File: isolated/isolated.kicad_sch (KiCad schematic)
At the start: 59 parts, among them J1 Screw_Terminal_01x02, J2 Screw_Terminal_01x02, Q1 IRLIZ 34N, Q2 IRLIZ 34N, U1 LTC3723, U2 TCMT1103, U3 TL431DBZ

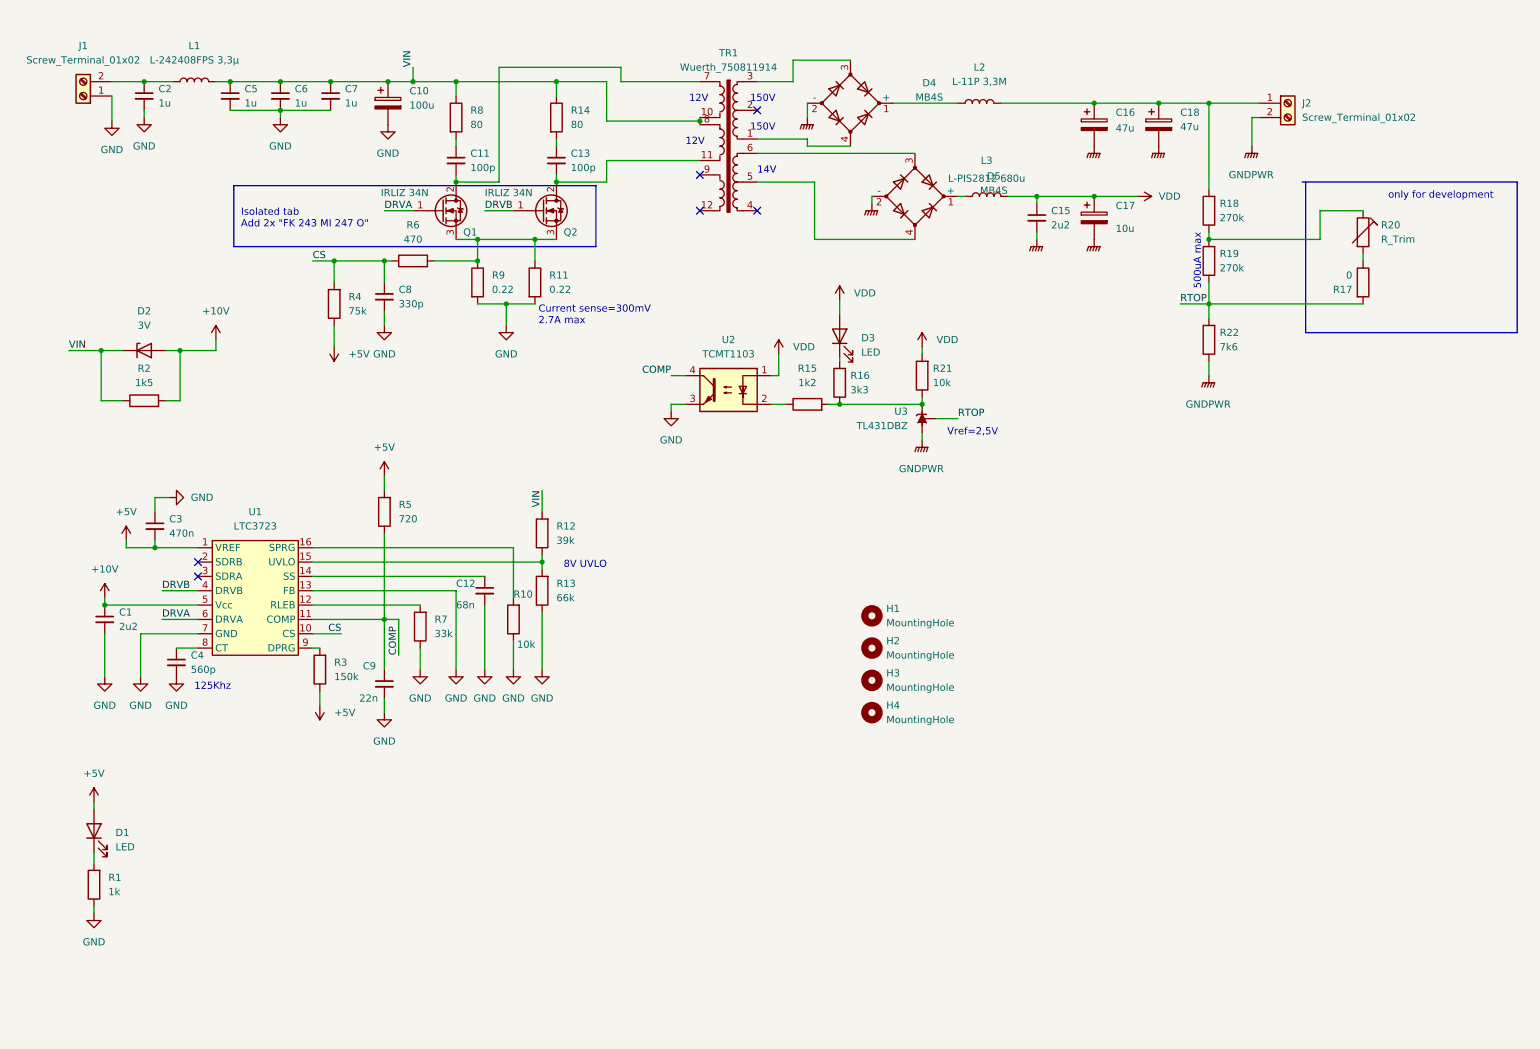
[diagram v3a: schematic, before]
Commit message: doc/kicad: Update to revision v0.2
Fix the problems found in revision v0.1.

Revision v0.2 works much better and is able to power a
4W 240VAC LED bulb using 270VDC.

There are a couple of things to improve though.

Signed-off-by: Patrick Rudolph <rudolphpatrick05@gmail.com>
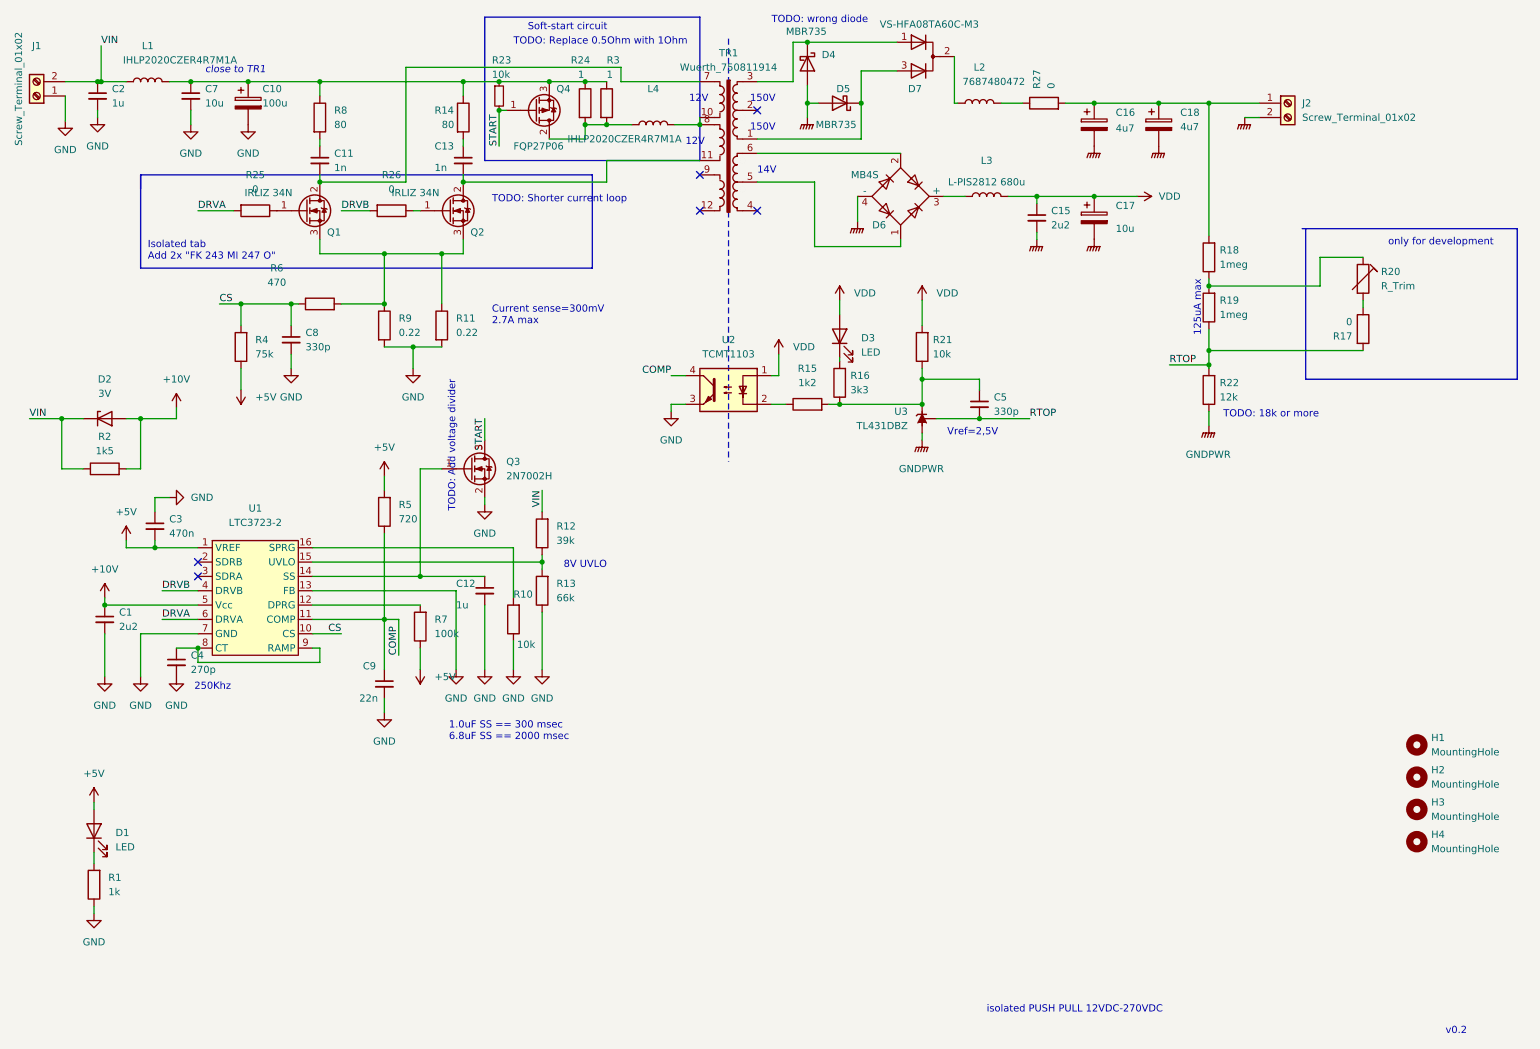
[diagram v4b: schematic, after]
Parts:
- removed C6: 1u, Capacitor_SMD:C_1210_3225Metric_Pad1.33x2.70mm_HandSolder, symbol Device:C_Small
- removed D4, D5: MB4S, Package_TO_SOT_SMD:TO-269AA, symbol Device:D_Bridge_+-AA
- removed U1: LTC3723, Package_SO:SSOP-16_3.9x4.9mm_P0.635mm, symbol LTC3723:LTC3723
- added D4, D5: MBR735, Package_TO_SOT_THT:TO-220-2_Vertical, symbol Diode:MBR735
- added D6: MB4S, Package_TO_SOT_SMD:TO-269AA, symbol Diode_Bridge:MB4S
- added D7: VS-HFA08TA60C-M3, Package_TO_SOT_THT:TO-220-3_Vertical, symbol Device:D_Dual_CommonCathode_AKA_Parallel
- added L4: IHLP2020CZER4R7M1A, Inductor_SMD:L_Sunlord_MWSA05xxS, symbol Device:L
- added Q3: 2N7002H, Package_TO_SOT_SMD:SOT-23, symbol Transistor_FET:2N7002H
- added Q4: FQP27P06, Package_TO_SOT_THT:TO-220-3_Vertical, symbol Transistor_FET:FQP27P06
- added R23: 10k, Resistor_SMD:R_0805_2012Metric_Pad1.20x1.40mm_HandSolder, symbol Device:R_Small
- added R24: 1, Resistor_SMD:R_1206_3216Metric_Pad1.30x1.75mm_HandSolder, symbol Device:R
- added R25, R26: 0, Resistor_SMD:R_0805_2012Metric_Pad1.20x1.40mm_HandSolder, symbol Device:R
- added R27: 0, Resistor_SMD:R_1206_3216Metric_Pad1.30x1.75mm_HandSolder, symbol Device:R
- added U1: LTC3723-2, Package_SO:SSOP-16_3.9x4.9mm_P0.635mm, symbol LTC3723:LTC3723-2
- C11, C13: value 100p -> 1n; footprint Capacitor_SMD:C_0603_1608Metric_Pad1.08x0.95mm_HandSolder -> Capacitor_SMD:C_0805_2012Metric_Pad1.18x1.45mm_HandSolder
- C12: value 68n -> 1u; footprint Capacitor_SMD:C_0603_1608Metric_Pad1.08x0.95mm_HandSolder -> Capacitor_SMD:C_1210_3225Metric_Pad1.33x2.70mm_HandSolder
- C16, C18: value 47u -> 4u7
- C4: value 560p -> 270p
- C5: value 1u -> 330p; footprint Capacitor_SMD:C_1210_3225Metric_Pad1.33x2.70mm_HandSolder -> Capacitor_SMD:C_0603_1608Metric_Pad1.08x0.95mm_HandSolder
- C7: value 1u -> 10u
- L1: value L-242408FPS 3,3µ -> IHLP2020CZER4R7M1A; footprint Inductor_SMD:L_Ferrocore_DLG-0504 -> Inductor_SMD:L_Sunlord_MWSA05xxS
- L2: value L-11P 3,3M -> 7687480472
- R14, R8: footprint Resistor_SMD:R_0805_2012Metric_Pad1.20x1.40mm_HandSolder -> Resistor_SMD:R_1206_3216Metric_Pad1.30x1.75mm_HandSolder
- R18, R19: value 270k -> 1meg
- R22: value 7k6 -> 12k
- R3: value 150k -> 1; footprint Resistor_SMD:R_0805_2012Metric_Pad1.20x1.40mm_HandSolder -> Resistor_SMD:R_1206_3216Metric_Pad1.30x1.75mm_HandSolder
- R7: value 33k -> 100k
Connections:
- net +10V: now also U1.5 (Vcc)
- net +5V: now also R7.1, U1.1 (VREF); no longer R3.1
- net COMP: now also U1.11 (COMP)
- net CS: now also U1.10 (CS)
- net DRVA: now also R25.2, U1.6 (DRVA); no longer Q1.1 (G)
- net DRVB: now also R26.2, U1.4 (DRVB); no longer Q2.1 (G)
- net GND: now also Q3.2 (S), U1.13 (FB), U1.7 (GND); no longer C5.2, R7.1
- net GNDPWR: now also D4.2 (A), D5.2 (A), D6.4 (-)
- net RTOP: now also C5.2
- net VIN: now also C2.1, J1.2 (Pin_2), L1.1; no longer C10.1, C5.1, C7.1, L1.2, R14.1, R8.1, TR1.10, TR1.8
- net at R7.2: now also U1.12 (DPRG)
- net at C12.1: now also Q3.1 (G), U1.14 (SS)
- net at R12.1, R13.2: now also U1.15 (UVLO)
- net at R10.2: now also U1.16 (SPRG)
- net at C4.1: now also U1.8 (CT), U1.9 (RAMP)
- net at R3.2: now also L4.1, Q4.2 (D), R24.2
- net at R15.2, R16.1, R21.1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: now also C5.1
- net at C16.1, C18.1, J2.1 (Pin_1)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: now also R27.2; no longer L2.2
- net at L3.1: now also D6.3 (+)
- net at TR1.6: now also D6.2
- net at TR1.5: now also D6.1
- net at L2.1: now also D7.2 (A)
- net at TR1.3: now also D4.1 (K), D7.1 (K)
- net at TR1.1: now also D5.1 (K), D7.3 (K)
- new net: C10.1, C7.1, L1.2, Q4.3 (S), R14.1, R23.1, R24.1, R3.1, R8.1
- new net: Q1.1 (G), R25.1
- new net: L2.2, R27.1
- new net: Q2.1 (G), R26.1
- new net: L4.2, TR1.10, TR1.8
- new net START: Q3.3 (D), Q4.1 (G), R23.2
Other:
- note added: "1.0uF SS == 300 msec 6.8uF SS == 2000 msec"
- note added: "125uA max"
- note added: "250Khz"
- note added: "Soft-start circuit"
- note added: "TODO: 18k or more"
- note added: "TODO: Add voltage divider"
- note added: "TODO: Replace 0.5Ohm with 1Ohm"
- note added: "TODO: Shorter current loop"
- note added: "TODO: wrong diode"
- note added: "close to TR1"
- note added: "isolated PUSH PULL 12VDC-270VDC"
- note added: "v0.2"
- note removed: "125Khz"
- note removed: "500uA max"
- moved on the sheet: C10, C11, C13, C2, C7, C8, D2, H1, H2, H3, H4, J1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
